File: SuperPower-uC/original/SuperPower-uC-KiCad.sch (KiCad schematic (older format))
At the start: 2 parts, among them J10 Conn_01x12_Male, J9 Conn_01x12_Male

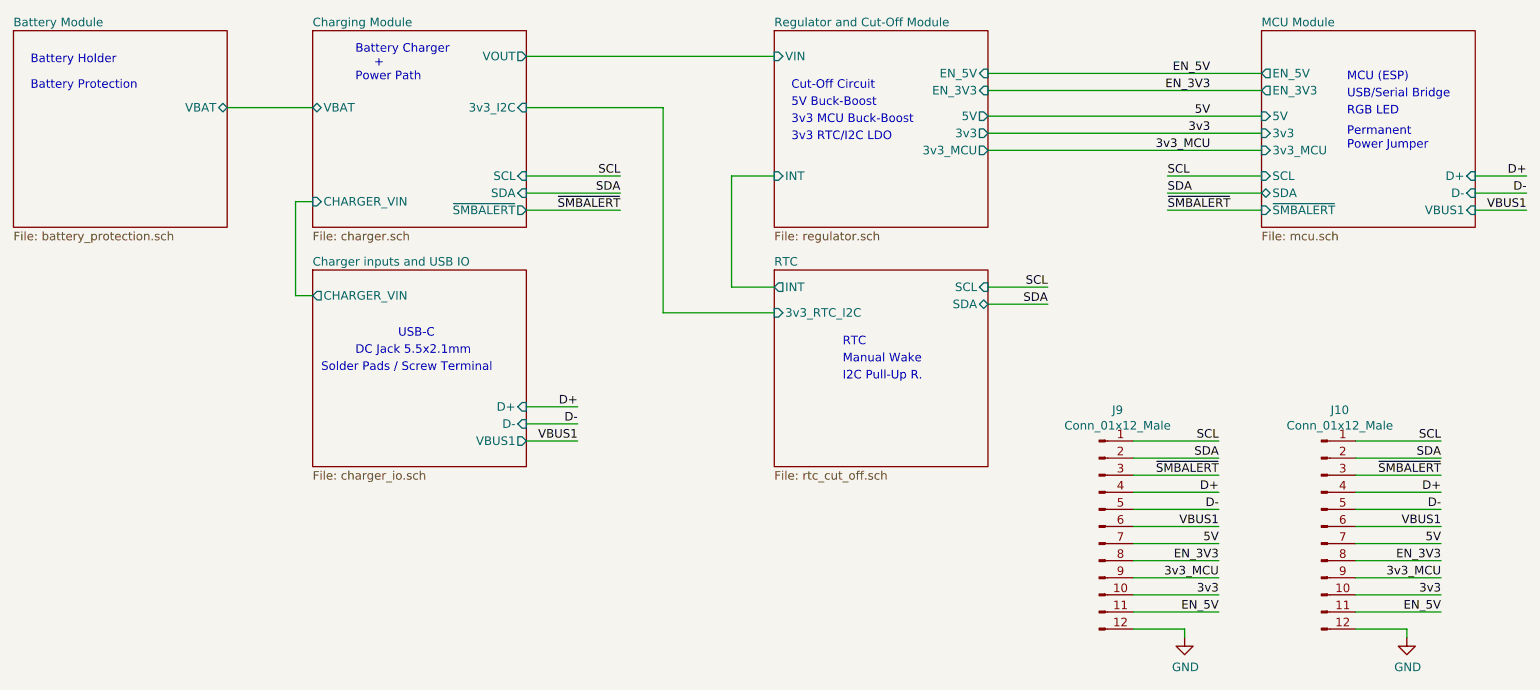
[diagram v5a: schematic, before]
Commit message: Removed 0R from USB-C VBUS because it can not be used as planned and has no function
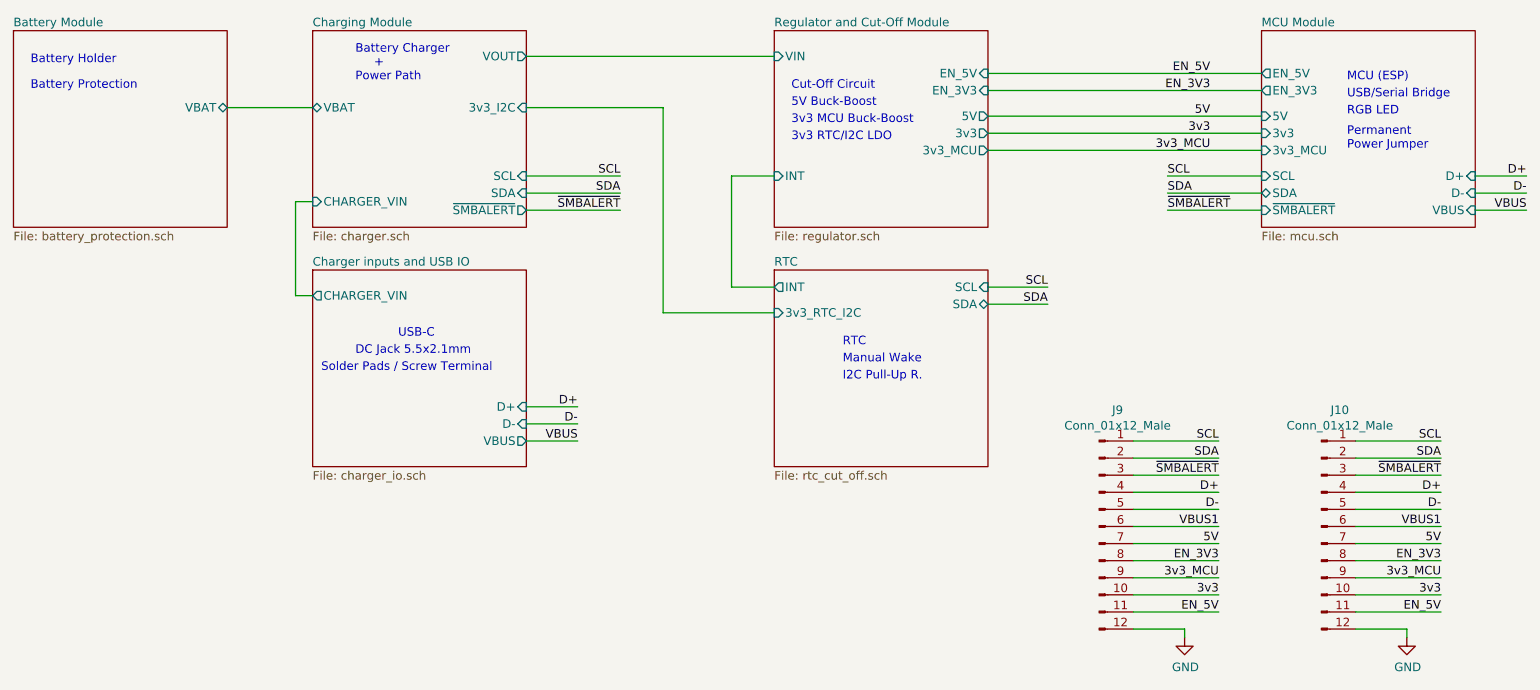
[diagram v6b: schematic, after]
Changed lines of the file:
@@
 F3 "D-" I R 4300 4400 50
 F4 "CHARGER_VIN" O L 3050 3650 50
-F5 "VBUS1" O R 4300 4500 50
+F5 "VBUS" O R 4300 4500 50
 $EndSheet
 Wire Wire Line
@@
 	4850 3150 4300 3150
 Text Label 4600 4500 2    50   ~ 0
-VBUS1
+VBUS
 Text Label 4600 4400 2    50   ~ 0
 D-
@@
 	4600 4500 4300 4500
 Text Label 10150 3150 2    50   ~ 0
-VBUS1
+VBUS
 Text Label 10150 3050 2    50   ~ 0
 D-
@@
 F10 "EN_5V" O L 8600 2350 50
 F11 "~SMBALERT" I L 8600 3150 50
-F12 "VBUS1" I R 9850 3150 50
+F12 "VBUS" I R 9850 3150 50
 $EndSheet
 $Sheet

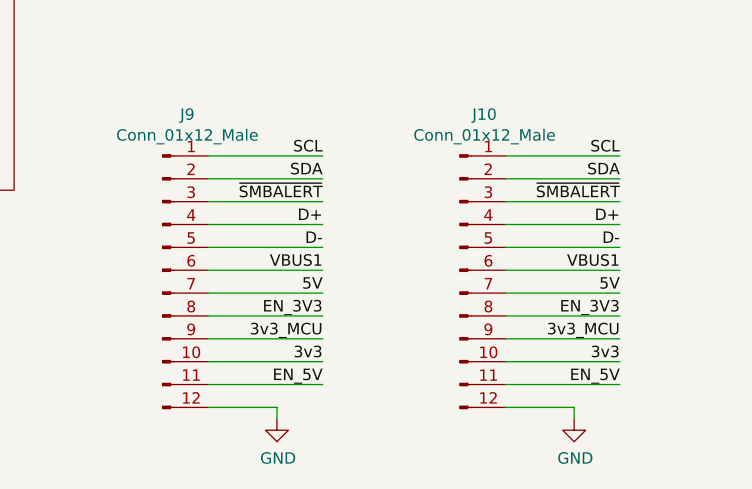
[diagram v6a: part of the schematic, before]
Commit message: Moving parts arround to find a nice fit
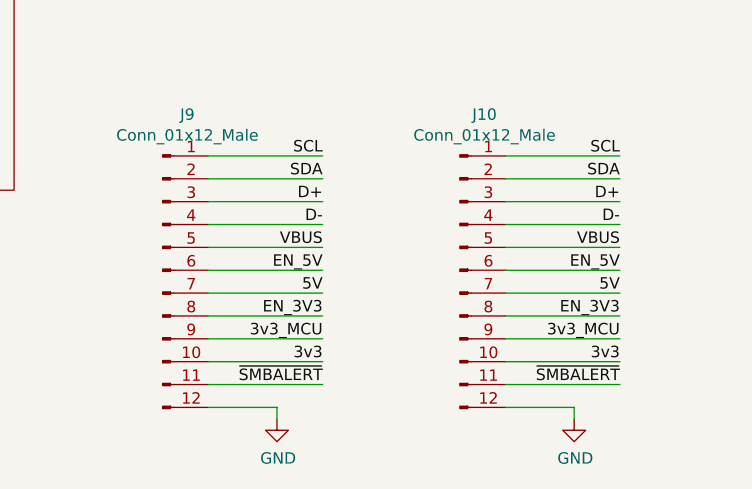
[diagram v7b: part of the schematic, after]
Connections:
- net VBUS1 is gone; now on net EN_5V: J10.6 (Pin_6), J9.6 (Pin_6)
- net D+: now also J10.3 (Pin_3), J9.3 (Pin_3); no longer J10.4 (Pin_4), J9.4 (Pin_4)
- net D-: now also J10.4 (Pin_4), J9.4 (Pin_4); no longer J10.5 (Pin_5), J9.5 (Pin_5)
- net EN_5V: no longer J10.11 (Pin_11), J9.11 (Pin_11)
- net VBUS: now also J10.5 (Pin_5), J9.5 (Pin_5)
- net ~SMBALERT: now also J10.11 (Pin_11), J9.11 (Pin_11); no longer J10.3 (Pin_3), J9.3 (Pin_3)
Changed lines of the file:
@@
 Text Label 8350 4600 2    50   ~ 0
 SDA
+Text Label 8350 5500 2    50   ~ 0
+~SMBALERT
 Text Label 8350 4700 2    50   ~ 0
-~SMBALERT
+D+
 Text Label 8350 4800 2    50   ~ 0
-D+
+D-
 Text Label 8350 4900 2    50   ~ 0
-D-
-Text Label 8350 5000 2    50   ~ 0
-VBUS1
+VBUS
 Text Label 8350 5400 2    50   ~ 0
 3v3
-Text Label 8350 5500 2    50   ~ 0
+Text Label 8350 5000 2    50   ~ 0
 EN_5V
 Text Label 8350 5200 2    50   ~ 0
@@
 Text Label 9650 4600 2    50   ~ 0
 SDA
+Text Label 9650 5500 2    50   ~ 0
+~SMBALERT
 Text Label 9650 4700 2    50   ~ 0
-~SMBALERT
+D+
 Text Label 9650 4800 2    50   ~ 0
-D+
+D-
 Text Label 9650 4900 2    50   ~ 0
-D-
-Text Label 9650 5000 2    50   ~ 0
-VBUS1
+VBUS
 Text Label 9650 5400 2    50   ~ 0
 3v3
-Text Label 9650 5500 2    50   ~ 0
+Text Label 9650 5000 2    50   ~ 0
 EN_5V
 Text Label 9650 5200 2    50   ~ 0

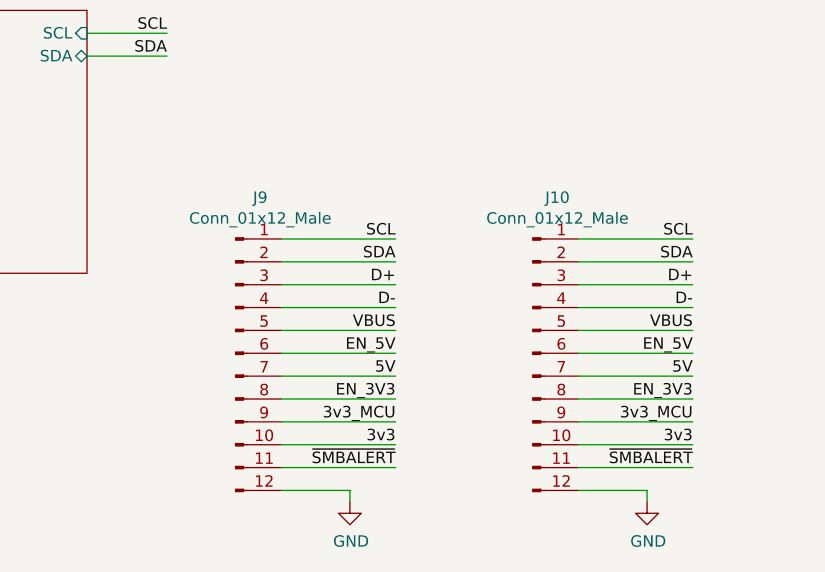
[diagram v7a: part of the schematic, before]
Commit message: Add GND to the interface connector
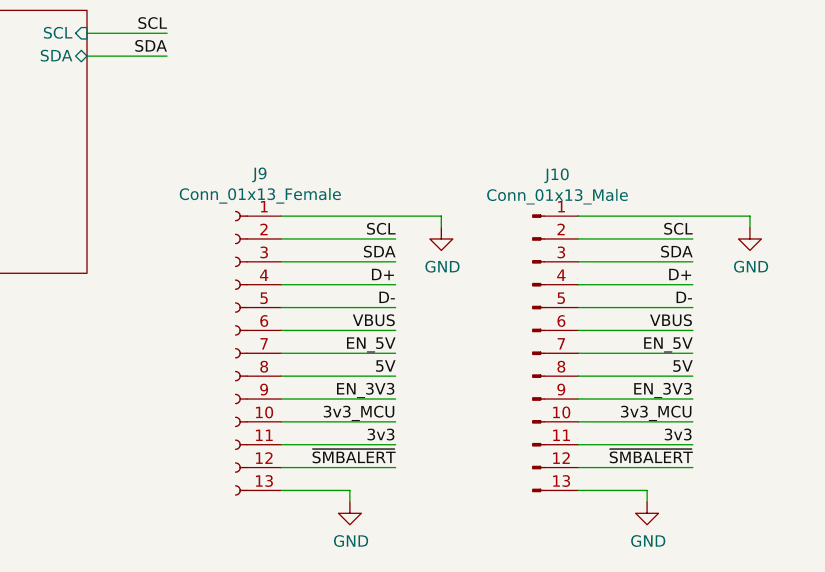
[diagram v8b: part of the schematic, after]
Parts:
- removed J10, J9: Conn_01x12_Male, Connector_PinSocket_2.54mm:PinSocket_1x12_P2.54mm_Vertical, symbol Connector:Conn_01x12_Male
- added J10: Conn_01x13_Male, Connector_PinSocket_2.54mm:PinSocket_1x13_P2.54mm_Vertical, symbol Connector:Conn_01x13_Male
- added J9: Conn_01x13_Female, Connector_PinHeader_2.54mm:PinHeader_1x13_P2.54mm_Vertical, symbol Connector:Conn_01x13_Female
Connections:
- net 3v3: now also J10.11 (Pin_11), J9.11 (Pin_11)
- net 3v3_MCU: now also J10.10 (Pin_10), J9.10 (Pin_10)
- net 5V: now also J10.8 (Pin_8), J9.8 (Pin_8)
- net D+: now also J10.4 (Pin_4), J9.4 (Pin_4)
- net D-: now also J10.5 (Pin_5), J9.5 (Pin_5)
- net EN_3V3: now also J10.9 (Pin_9), J9.9 (Pin_9)
- net EN_5V: now also J10.7 (Pin_7), J9.7 (Pin_7)
- net GND: now also J10.1 (Pin_1), J10.13 (Pin_13), J9.1 (Pin_1), J9.13 (Pin_13)
- net SCL: now also J10.2 (Pin_2), J9.2 (Pin_2)
- net SDA: now also J10.3 (Pin_3), J9.3 (Pin_3)
- net VBUS: now also J10.6 (Pin_6), J9.6 (Pin_6)
- net ~SMBALERT: now also J10.12 (Pin_12), J9.12 (Pin_12)
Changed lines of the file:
@@
 3v3_MCU
-$Comp
-L Connector:Conn_01x12_Male J9
-U 1 1 5FE4755E
-P 7650 5000
-F 0 "J9" H 7758 5681 50  0000 C CNN
-F 1 "Conn_01x12_Male" H 7758 5590 50  0000 C CNN
-F 2 "Connector_PinSocket_2.54mm:PinSocket_1x12_P2.54mm_Vertical" H 7650 5000 50  0001 C CNN
-F 3 "~" H 7650 5000 50  0001 C CNN
-	1    7650 5000
-	1    0    0    -1
-$EndComp
 $Comp
 L power:GND #PWR0112
@@
 Wire Wire Line
 	8150 5600 7850 5600
-$Comp
-L Connector:Conn_01x12_Male J10
-U 1 1 5FE627D1
-P 8950 5000
-F 0 "J10" H 9058 5681 50  0000 C CNN
-F 1 "Conn_01x12_Male" H 9058 5590 50  0000 C CNN
-F 2 "Connector_PinSocket_2.54mm:PinSocket_1x12_P2.54mm_Vertical" H 8950 5000 50  0001 C CNN
-F 3 "~" H 8950 5000 50  0001 C CNN
-	1    8950 5000
-	1    0    0    -1
-$EndComp
 Text Label 9650 4500 2    50   ~ 0
 SCL
@@
 Wire Wire Line
 	9450 5600 9150 5600
+$Comp
+L Connector:Conn_01x13_Female J9
+U 1 1 600940E1
+P 7650 5000
+F 0 "J9" H 7542 5785 50  0000 C CNN
+F 1 "Conn_01x13_Female" H 7542 5694 50  0000 C CNN
+F 2 "Connector_PinHeader_2.54mm:PinHeader_1x13_P2.54mm_Vertical" H 7650 5000 50  0001 C CNN
+F 3 "~" H 7650 5000 50  0001 C CNN
+	1    7650 5000
+	-1   0    0    -1
+$EndComp
+$Comp
+L Connector:Conn_01x13_Male J10
+U 1 1 600965AF
+P 8950 5000
+F 0 "J10" H 9058 5781 50  0000 C CNN
+F 1 "Conn_01x13_Male" H 9058 5690 50  0000 C CNN
+F 2 "Connector_PinSocket_2.54mm:PinSocket_1x13_P2.54mm_Vertical" H 8950 5000 50  0001 C CNN
+F 3 "~" H 8950 5000 50  0001 C CNN
+	1    8950 5000
+	1    0    0    -1
+$EndComp
+$Comp
+L power:GND #PWR0109
+U 1 1 6009915B
+P 9900 4450
+F 0 "#PWR0109" H 9900 4200 50  0001 C CNN
+F 1 "GND" H 9905 4277 50  0000 C CNN
+F 2 "" H 9900 4450 50  0001 C CNN
+F 3 "" H 9900 4450 50  0001 C CNN
+	1    9900 4450
+	1    0    0    -1
+$EndComp
+$Comp
+L power:GND #PWR0111
+U 1 1 60099602
+P 8550 4450
+F 0 "#PWR0111" H 8550 4200 50  0001 C CNN
+F 1 "GND" H 8555 4277 50  0000 C CNN
+F 2 "" H 8550 4450 50  0001 C CNN
+F 3 "" H 8550 4450 50  0001 C CNN
+	1    8550 4450
+	1    0    0    -1
+$EndComp
+Wire Wire Line
+	9150 4400 9900 4400
+Wire Wire Line
+	9900 4400 9900 4450
+Wire Wire Line
+	7850 4400 8550 4400
+Wire Wire Line
+	8550 4400 8550 4450
 $EndSCHEMATC
